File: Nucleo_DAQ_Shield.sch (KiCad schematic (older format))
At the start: 33 parts, among them J1 CONN_01X05, J2 CONN_01X06, J3 CONN_01X02, J5 CONN_01X10, J6 CONN_COAXIAL, J8 CONN_02X04, J9 CONN_01X04, U1 4050, U10 ST_Nucleo144_F746ZG_CN10, U2 TL072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

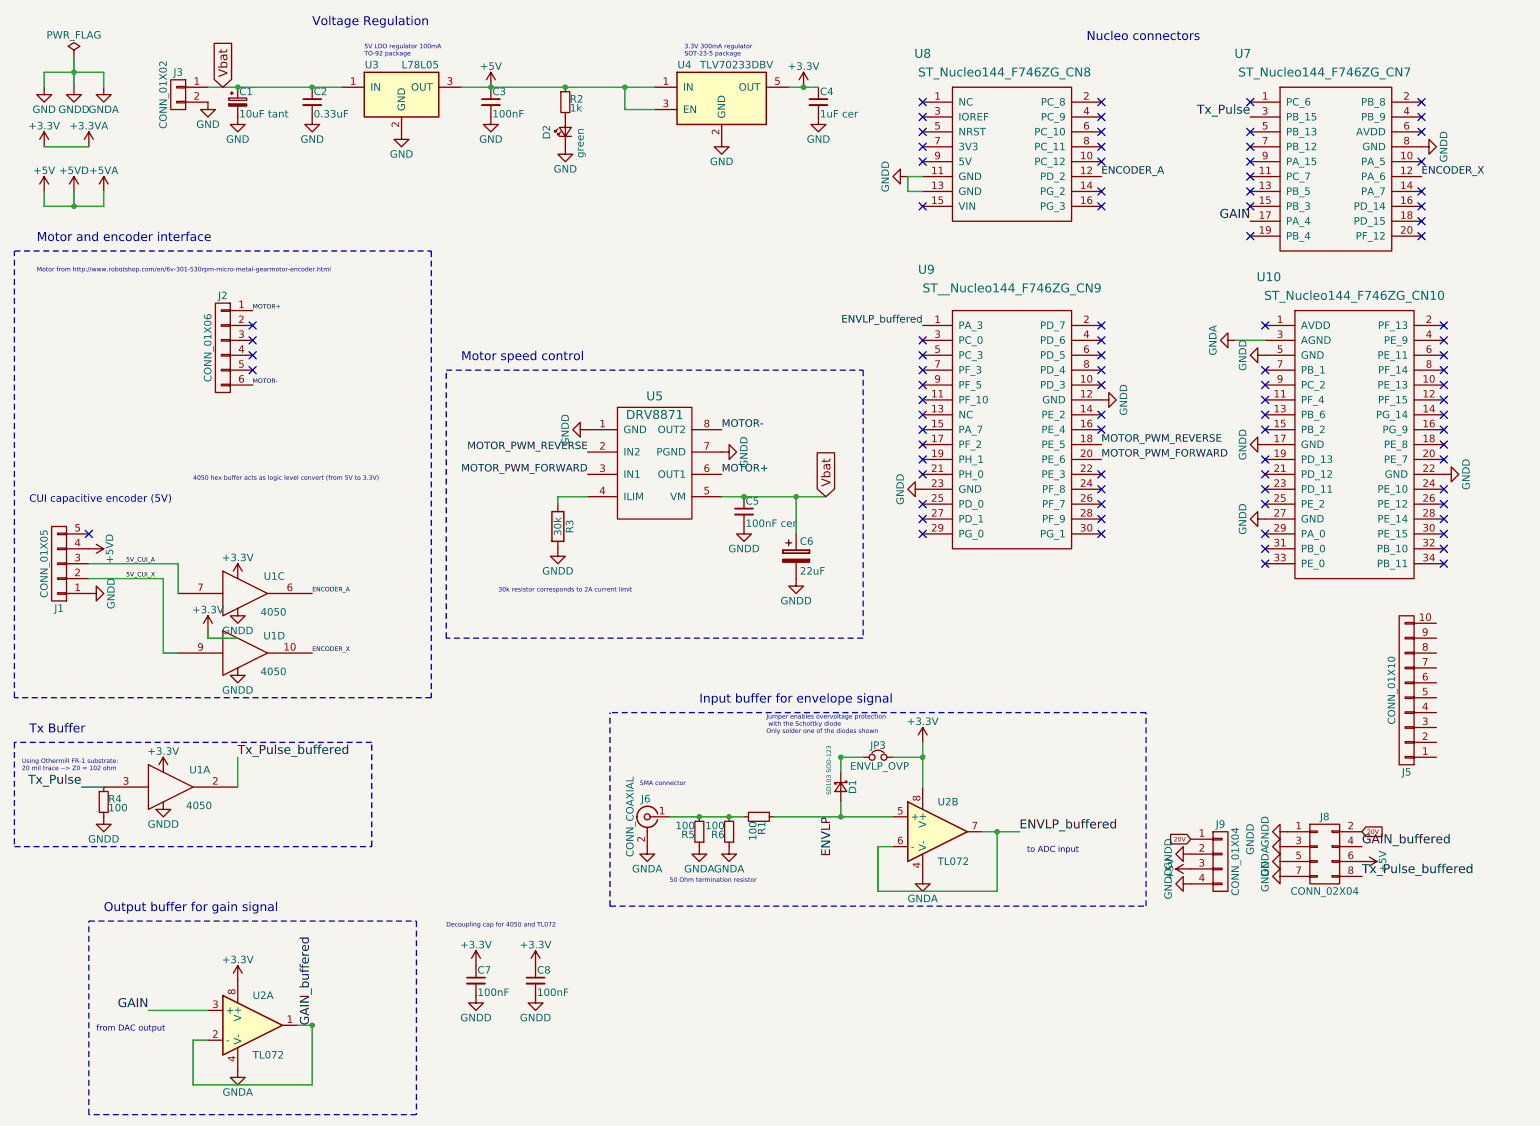
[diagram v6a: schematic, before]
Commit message: Updated IMU connector and encoder pins
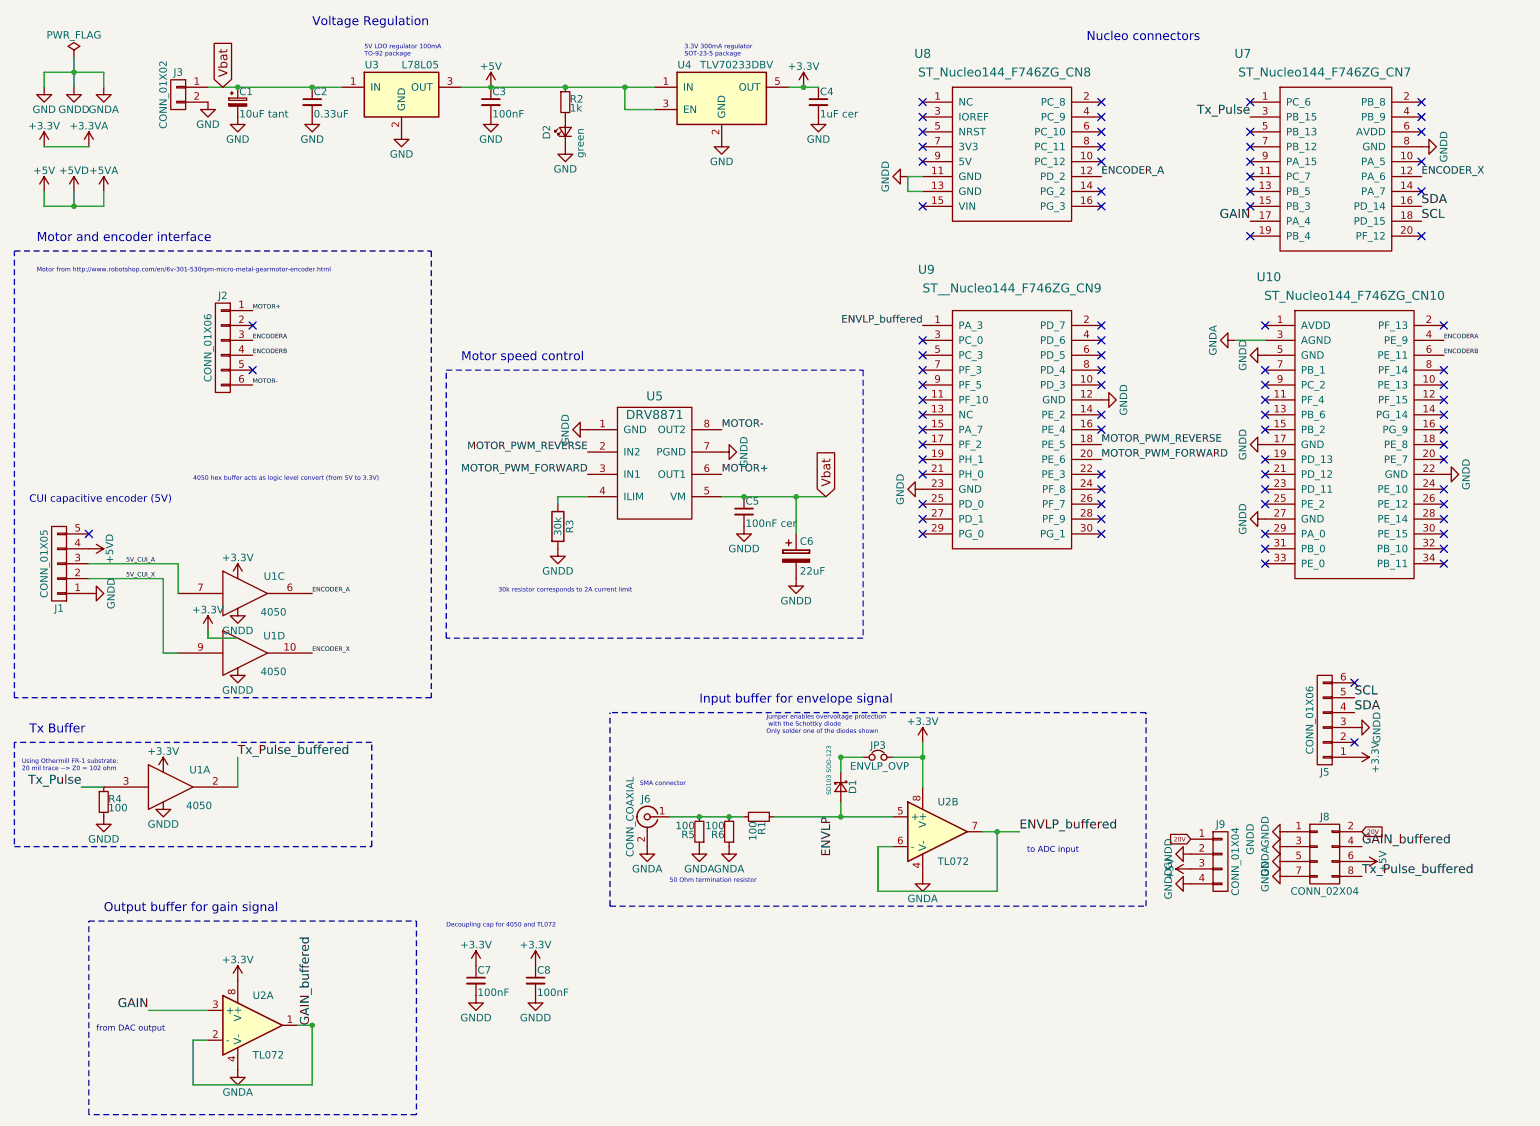
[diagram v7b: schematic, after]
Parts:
- removed J5: CONN_01X10, Pin_Headers:Pin_Header_Angled_1x10_Pitch2.54mm, symbol CONN_01X10
- added J5: CONN_01X06, Pin_Headers:Pin_Header_Straight_1x06_Pitch2.54mm, symbol CONN_01X06
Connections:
- net +3.3VA: now also J5.1 (P1)
- net GND: now also J5.3 (P3)
- net ENCODERA: now reaches J2.3 (P3)
- net ENCODERA: now also U10.4 (PE_9)
- net ENCODERB: now reaches J2.4 (P4)
- net ENCODERB: now also U10.6 (PE_11)
- net SDA: now reaches U7.16 (PD_14)
- net SDA: now also J5.4 (P4)
- net SCL: now reaches U7.18 (PD_15)
- net SCL: now also J5.5 (P5)
- no-connect marks 88 -> 84
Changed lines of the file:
@@
-$EndComp
-$Comp
-L ST_Nucleo144_F746ZG_CN7 U7
-U 1 1 59646625
-P 9450 1450
-F 0 "U7" H 8850 2125 60  0000 C CNN
-F 1 "ST_Nucleo144_F746ZG_CN7" H 9400 2000 60  0000 C CNN
-F 2 "Pin_Headers:Pin_Header_Straight_2x10_Pitch2.54mm" H 9350 650 60  0001 C CNN
-F 3 "" H 9350 650 60  0001 C CNN
-	1    9450 1450
-	1    0    0    -1
 $EndComp
 $Comp
@@
 5V_CUI_X
 NoConn ~ 2200 2600
-NoConn ~ 2200 2700
-NoConn ~ 2200 2800
 NoConn ~ 2200 2900
 $Comp
@@
 NoConn ~ 10050 1500
 NoConn ~ 10050 1700
-NoConn ~ 10050 1800
-NoConn ~ 10050 1900
+NoConn ~ 9600 5000
 NoConn ~ 10050 2000
 NoConn ~ 6700 2700
@@
 NoConn ~ 9000 4200
 NoConn ~ 10200 2600
-NoConn ~ 10200 2700
-NoConn ~ 10200 2800
 NoConn ~ 10200 2900
 NoConn ~ 10200 3000
@@
 5V LDO regulator 100mA\nTO-92 package
 $Comp
-L CONN_01X10 J5
-U 1 1 59E7F53F
-P 9950 5050
-F 0 "J5" H 9950 5600 50  0000 C CNN
-F 1 "CONN_01X10" V 10050 5050 50  0000 C CNN
-F 2 "Pin_Headers:Pin_Header_Angled_1x10_Pitch2.54mm" H 9950 5050 50  0001 C CNN
-F 3 "" H 9950 5050 50  0001 C CNN
-	1    9950 5050
-	-1   0    0    1
-$EndComp
-$Comp
 L CONN_02X04 J8
 U 1 1 59E82128
@@
 	-1   0    0    1
 $EndComp
+$Comp
+L CONN_01X06 J5
+U 1 1 5A00D711
+P 9400 5250
+F 0 "J5" H 9400 5600 50  0000 C CNN
+F 1 "CONN_01X06" V 9500 5250 50  0000 C CNN
+F 2 "Pin_Headers:Pin_Header_Straight_1x06_Pitch2.54mm" H 9400 5250 50  0001 C CNN
+F 3 "" H 9400 5250 50  0001 C CNN
+	1    9400 5250
+	-1   0    0    1
+$EndComp
+$Comp
+L +3.3V #PWR062
+U 1 1 5A00DF53
+P 9600 5500
+F 0 "#PWR062" H 9600 5350 50  0001 C CNN
+F 1 "+3.3V" H 9600 5640 50  0000 C CNN
+F 2 "" H 9600 5500 50  0001 C CNN
+F 3 "" H 9600 5500 50  0001 C CNN
+	1    9600 5500
+	0    1    1    0
+$EndComp
+$Comp
+L GNDD #PWR063
+U 1 1 5A00E061
+P 9600 5300
+F 0 "#PWR063" H 9600 5050 50  0001 C CNN
+F 1 "GNDD" H 9600 5150 50  0000 C CNN
+F 2 "" H 9600 5300 50  0001 C CNN
+F 3 "" H 9600 5300 50  0001 C CNN
+	1    9600 5300
+	0    -1   -1   0
+$EndComp
+$Comp
+L ST_Nucleo144_F746ZG_CN7 U7
+U 1 1 59646625
+P 9450 1450
+F 0 "U7" H 8850 2125 60  0000 C CNN
+F 1 "ST_Nucleo144_F746ZG_CN7" H 9400 2000 60  0000 C CNN
+F 2 "Pin_Headers:Pin_Header_Straight_2x10_Pitch2.54mm" H 9350 650 60  0001 C CNN
+F 3 "" H 9350 650 60  0001 C CNN
+	1    9450 1450
+	1    0    0    -1
+$EndComp
+Text Label 10050 1800 0    60   ~ 0
+SDA
+Text Label 9600 5200 0    60   ~ 0
+SDA
+Text Label 10050 1900 0    60   ~ 0
+SCL
+Text Label 9600 5100 0    60   ~ 0
+SCL
+NoConn ~ 9600 5400
+Text Label 2200 2700 0    30   ~ 0
+ENCODERA
+Text Label 2200 2800 0    30   ~ 0
+ENCODERB
+Text Label 10200 2700 0    30   ~ 0
+ENCODERA
+Text Label 10200 2800 0    30   ~ 0
+ENCODERB
 $EndSCHEMATC

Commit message: Necleo board encoder switch
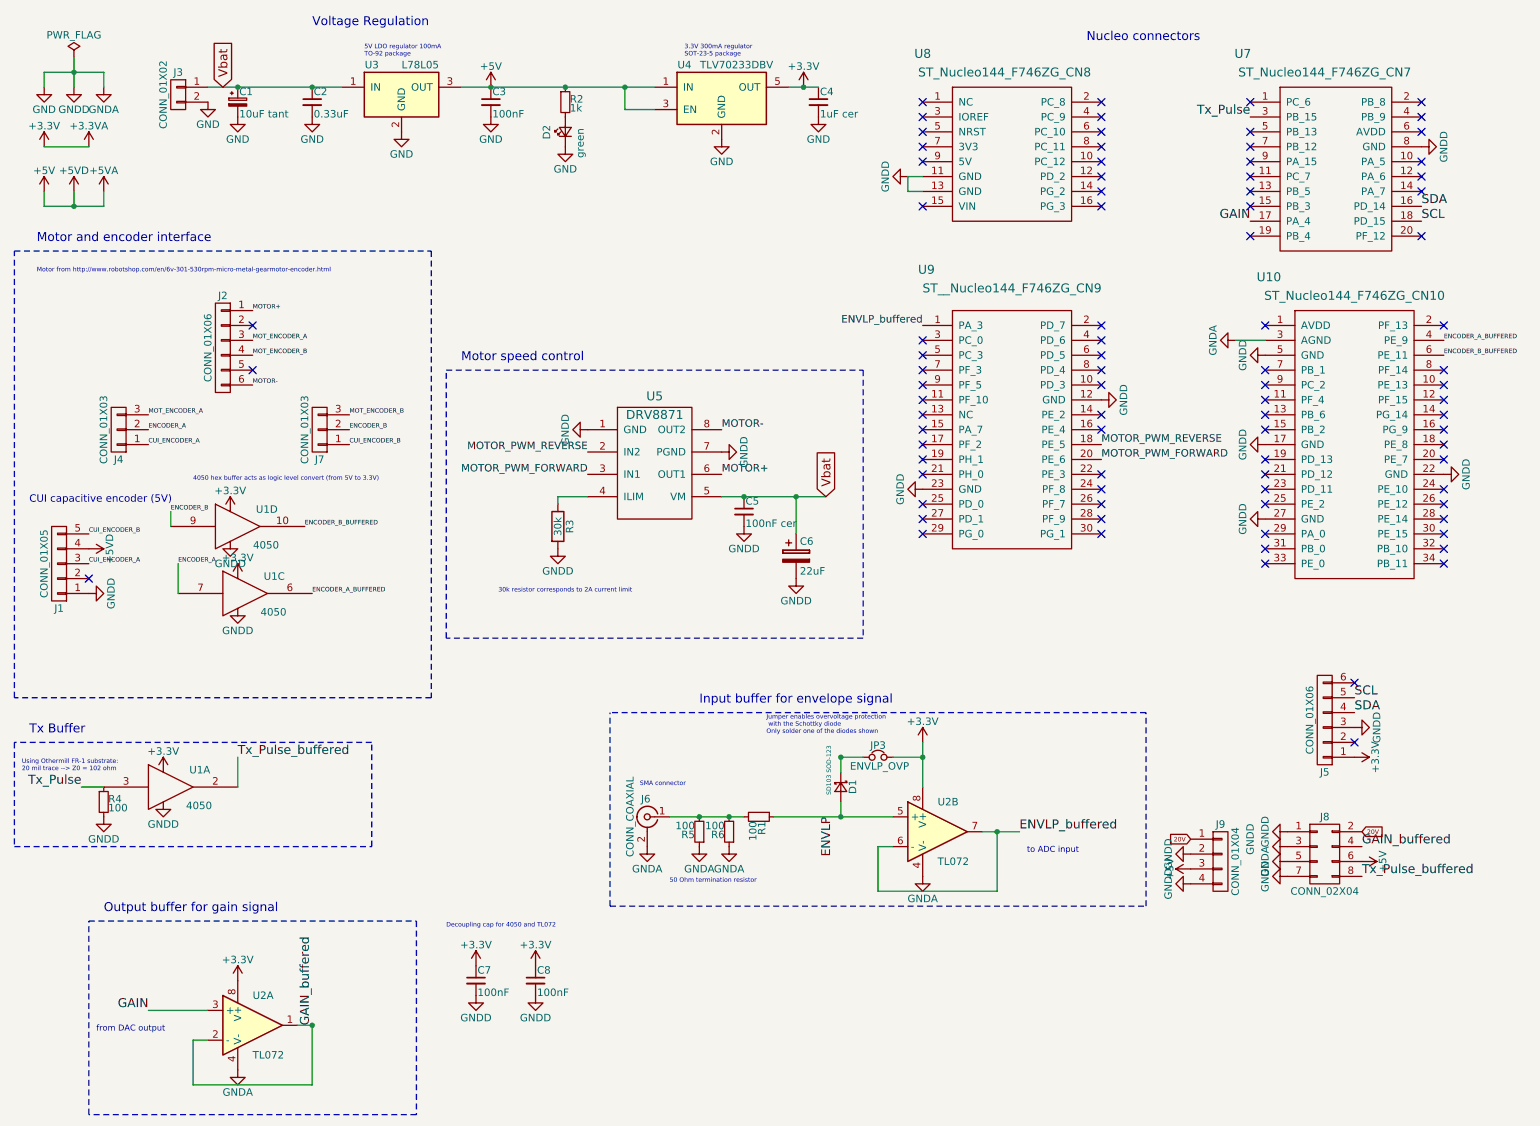
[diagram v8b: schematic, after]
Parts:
- added J4, J7: CONN_01X03, Pin_Headers:Pin_Header_Straight_1x03_Pitch2.54mm, symbol CONN_01X03
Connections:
- net ENCODER_A: now also U1.7, J4.2 (P2); no longer U1.6, U8.12 (PD_2)
- net CUI_ENCODER_B: now reaches J1.5 (P5)
- net CUI_ENCODER_B: now also J7.1 (P1)
- net 5V_CUI_A renamed CUI_ENCODER_A
- net CUI_ENCODER_A: now also J4.1 (P1); no longer U1.7
- net 5V_CUI_X: no longer names the net of J1.2 (P2)
- net 5V_CUI_X: no longer U1.9
- net ENCODERA renamed ENCODER_A_BUFFERED
- net ENCODER_A_BUFFERED: now also U1.6; no longer J2.3 (P3)
- net ENCODERB renamed ENCODER_B_BUFFERED
- net ENCODER_B_BUFFERED: now also U1.10; no longer J2.4 (P4)
- net ENCODER_X: no longer names the net of U7.12 (PA_6)
- net ENCODER_X: no longer U1.10
- new net ENCODER_B: J7.2 (P2), U1.9
- new net MOT_ENCODER_A: J2.3 (P3), J4.3 (P3)
- new net MOT_ENCODER_B: J2.4 (P4), J7.3 (P3)
- no-connect marks 84 -> 86
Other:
- moved on the sheet: U1D
